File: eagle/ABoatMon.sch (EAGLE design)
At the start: 33 parts, among them J1 VUSB, J2 GND, J3 GND, J4 LIPO, J5 U.FL, X1 MKDSN1,5/2-5,08

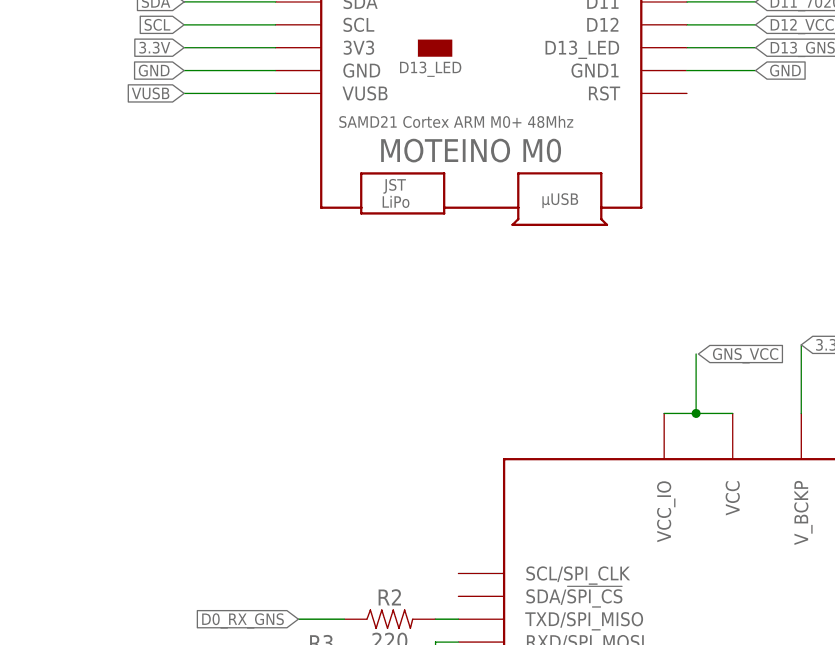
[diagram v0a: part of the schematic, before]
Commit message: Started R0.9 1. Mounting hole wrong place 2. Regulator board needs to move down due to overlapping edge of casterlated holes 3. Mobile module needs to move right 1mm due to sharp lower left edge hitting box 4. Need to move Ufl connector left due to grommets in box 5. Can make the edge tabs slightly deeper, will help routing 6. Need to add lipo connector and route to VUSB 7. Need to move Capacitor below regulator board
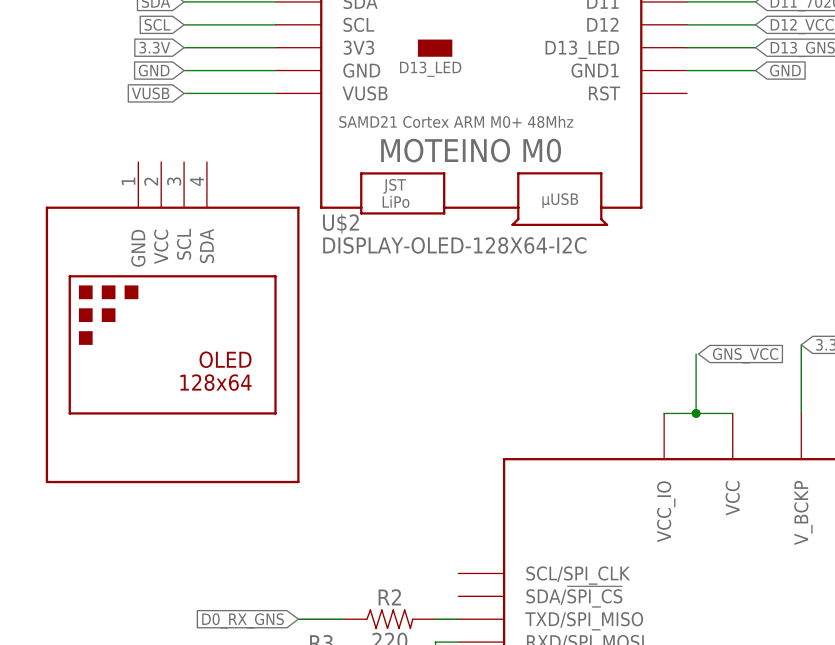
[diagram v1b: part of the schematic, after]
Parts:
- added U$2: DISPLAY-OLED-128X64-I2C, diy-modules:DISPLAY-OLED-128X64-I2C
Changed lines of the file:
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@@
 <part name="EXT_A" library="SparkFun-Connectors" library_urn="urn:adsk.eagle:library:513" deviceset="CONN_02" device="" package3d_urn="urn:adsk.eagle:package:38039/1"/>
 <part name="JST1" library="SparkFun-Connectors" library_urn="urn:adsk.eagle:library:513" deviceset="CONN_09" device="" package3d_urn="urn:adsk.eagle:package:38153/1"/>
+<part name="U$2" library="diy-modules" deviceset="DISPLAY-OLED-128X64-I2C" device=""/>
 </parts>
 <sheets>
@@
 <attribute name="NAME" x="139.7" y="150.368" size="1.778" layer="95" font="vector"/>
 </instance>
+<instance part="U$2" gate="G$1" x="22.86" y="91.44" smashed="yes">
+<attribute name="NAME" x="38.1" y="104.14" size="1.778" layer="95"/>
+<attribute name="VALUE" x="38.1" y="101.6" size="1.778" layer="96"/>
+</instance>
 </instances>

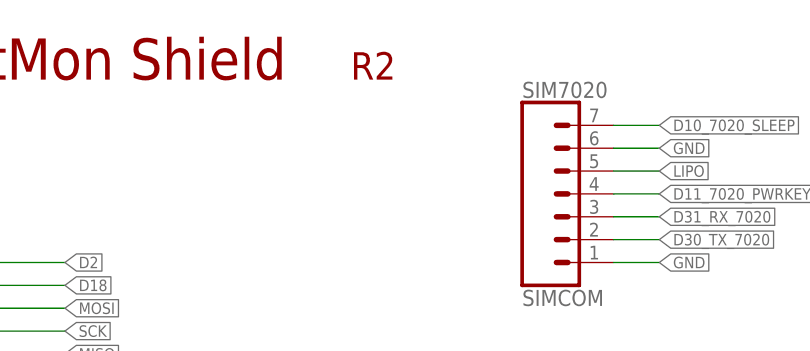
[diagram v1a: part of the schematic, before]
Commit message: Mounting hole and ufl moved
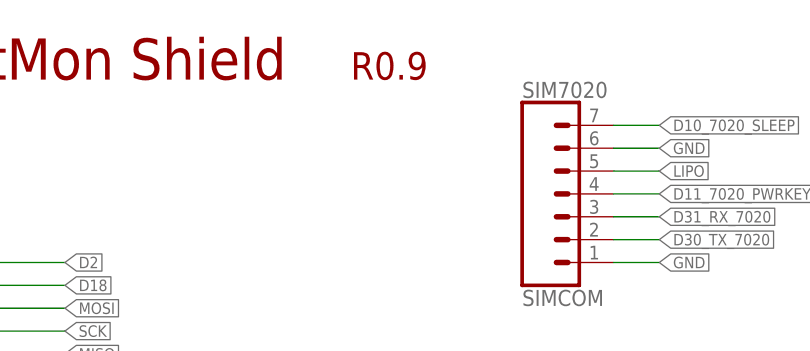
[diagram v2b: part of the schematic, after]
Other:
- note added: "R0.9"
- note removed: "R2"
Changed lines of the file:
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@@
 <?xml version="1.0" encoding="utf-8"?>
 <!DOCTYPE eagle SYSTEM "eagle.dtd">
-<eagle version="9.4.2">
+<eagle version="9.5.2">
 <drawing>
 <settings>
@@
 <attributes>
 <attribute name="CNAME" value="MoteinoMega ABoatMon Shield"/>
-<attribute name="CREVISION" value="0.899"/>
+<attribute name="CREVISION" value="0.9"/>
 <attribute name="DESIGNER" value="gregcope@gmail.com"/>
 </attributes>
@@
 Max 600mA 96% eff</text>
 <text x="101.6" y="162.56" size="3.048" layer="94" ratio="12">Greg Cope</text>
-<text x="189.23" y="167.64" size="3.048" layer="94" ratio="12">R2</text>
+<text x="189.23" y="167.64" size="3.048" layer="94" ratio="12">R0.9</text>
 <text x="101.6" y="167.64" size="4.572" layer="94" ratio="15">MoteinoM0 AboatMon Shield</text>
 <text x="187.96" y="25.4" size="1.27" layer="91">Consider MCP1810 lower shutdown current 1na</text>

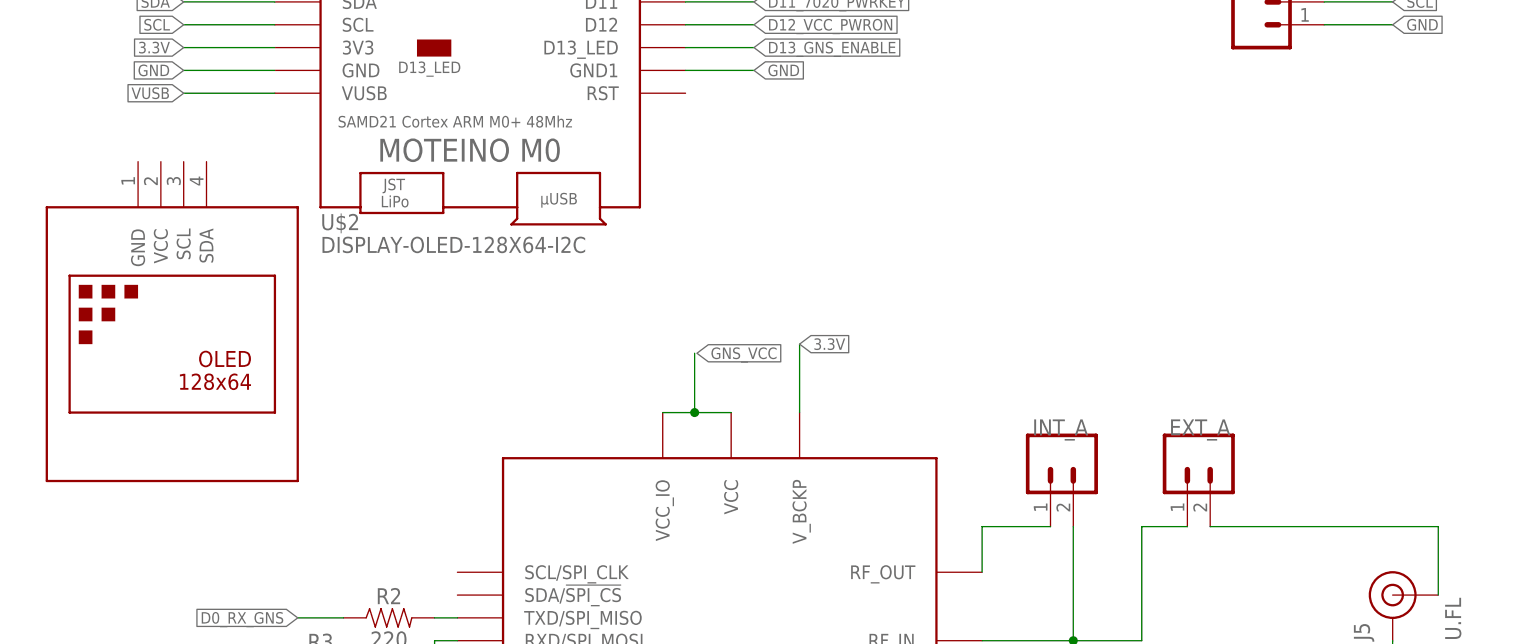
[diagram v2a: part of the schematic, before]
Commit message: pushed out tab sizes on either end
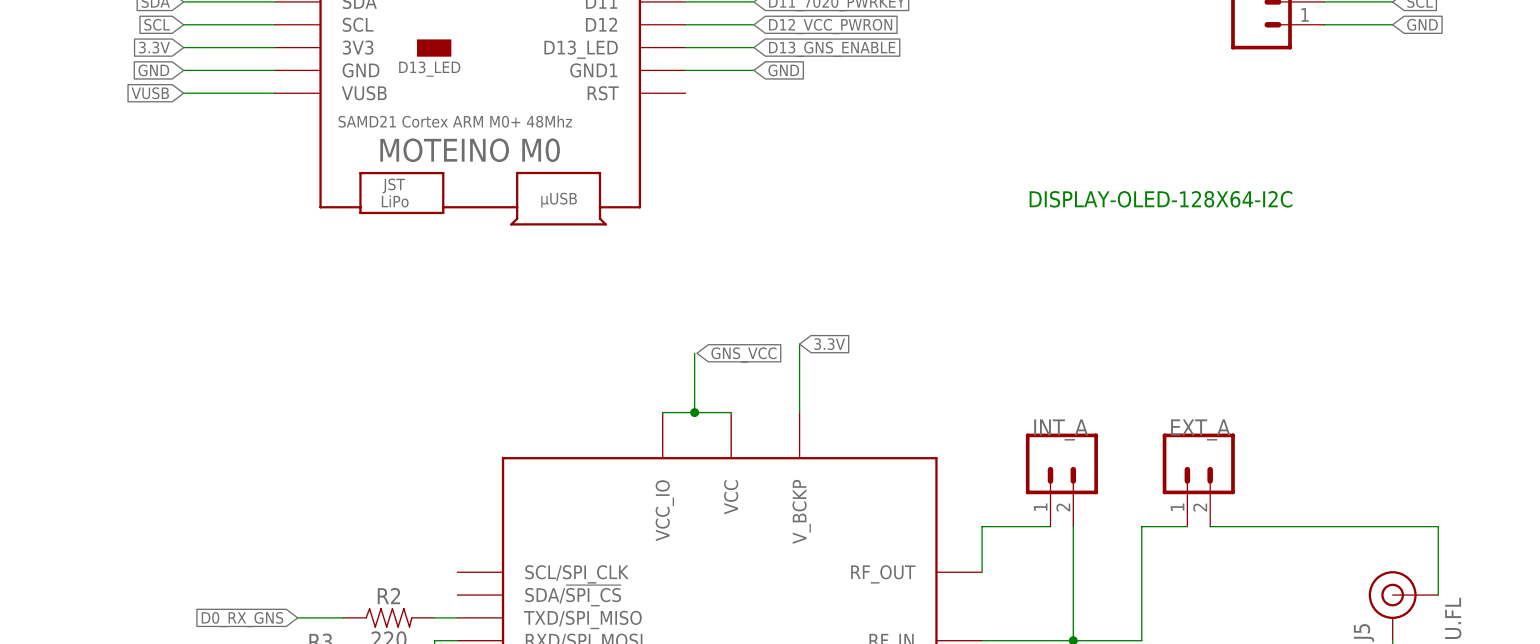
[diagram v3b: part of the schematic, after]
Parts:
- removed U$2: DISPLAY-OLED-128X64-I2C, diy-modules:DISPLAY-OLED-128X64-I2C
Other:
- note added: "DISPLAY-OLED-128X64-I2C"
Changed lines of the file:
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@@
 <part name="EXT_A" library="SparkFun-Connectors" library_urn="urn:adsk.eagle:library:513" deviceset="CONN_02" device="" package3d_urn="urn:adsk.eagle:package:38039/1"/>
 <part name="JST1" library="SparkFun-Connectors" library_urn="urn:adsk.eagle:library:513" deviceset="CONN_09" device="" package3d_urn="urn:adsk.eagle:package:38153/1"/>
-<part name="U$2" library="diy-modules" deviceset="DISPLAY-OLED-128X64-I2C" device=""/>
 </parts>
 <sheets>
@@
 <text x="187.96" y="25.4" size="1.27" layer="91">Consider MCP1810 lower shutdown current 1na</text>
 <text x="248.92" y="170.18" size="1.27" layer="91">VCC / GND Screw connector</text>
+<text x="116.84" y="106.68" size="1.778" layer="91">DISPLAY-OLED-128X64-I2C</text>
 </plain>
 <instances>
@@
 <attribute name="NAME" x="139.7" y="150.368" size="1.778" layer="95" font="vector"/>
 </instance>
-<instance part="U$2" gate="G$1" x="22.86" y="91.44" smashed="yes">
-<attribute name="NAME" x="38.1" y="104.14" size="1.778" layer="95"/>
-<attribute name="VALUE" x="38.1" y="101.6" size="1.778" layer="96"/>
-</instance>
 </instances>

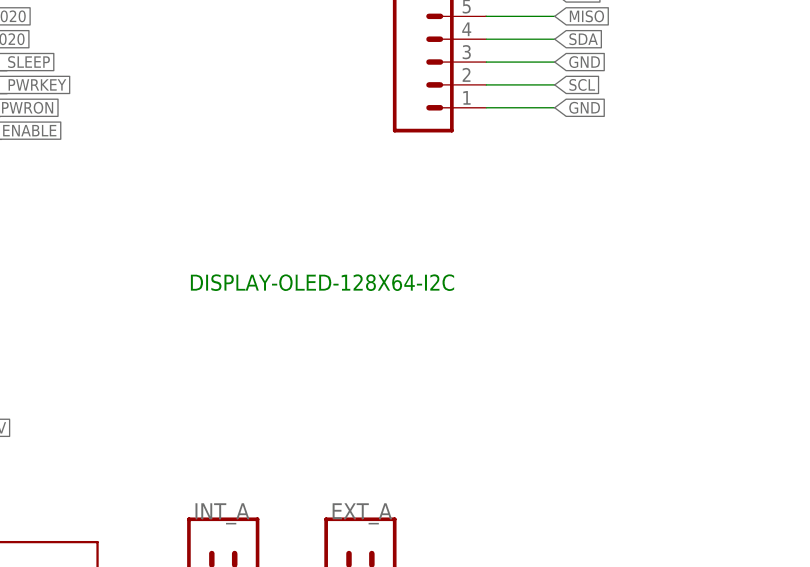
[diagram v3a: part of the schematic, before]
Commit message: removed wires
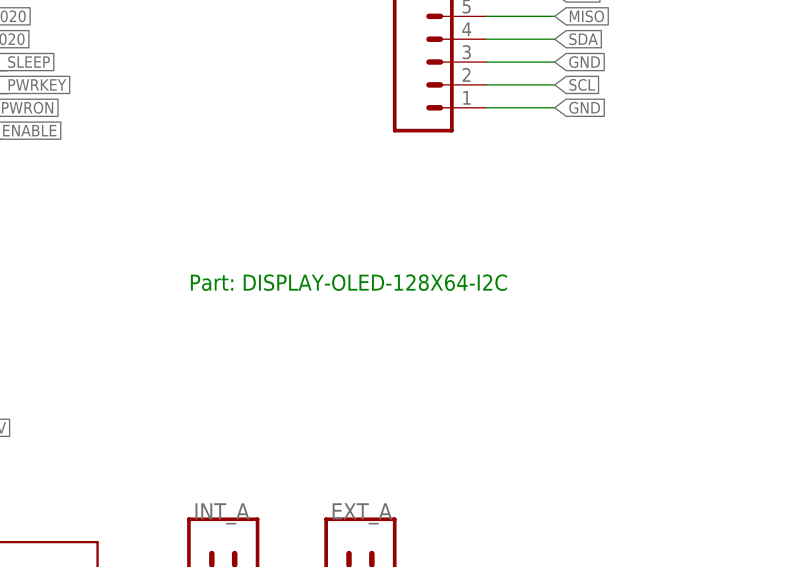
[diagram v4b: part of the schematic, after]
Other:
- note added: "Part: DISPLAY-OLED-128X64-I2C"
- note removed: "DISPLAY-OLED-128X64-I2C"
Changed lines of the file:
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@@
 <text x="187.96" y="25.4" size="1.27" layer="91">Consider MCP1810 lower shutdown current 1na</text>
 <text x="248.92" y="170.18" size="1.27" layer="91">VCC / GND Screw connector</text>
-<text x="116.84" y="106.68" size="1.778" layer="91">DISPLAY-OLED-128X64-I2C</text>
+<text x="116.84" y="106.68" size="1.778" layer="91">Part: DISPLAY-OLED-128X64-I2C</text>
 </plain>
 <instances>
